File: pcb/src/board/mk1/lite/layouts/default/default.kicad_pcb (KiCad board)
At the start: 2 copper layers, 21 parts

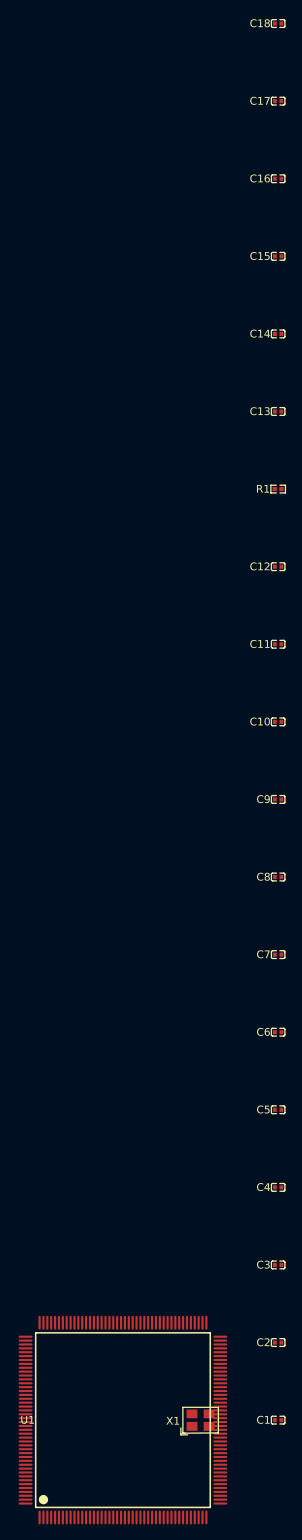
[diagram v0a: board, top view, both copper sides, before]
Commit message: pcb: add decoupling capacitors to STM32F429
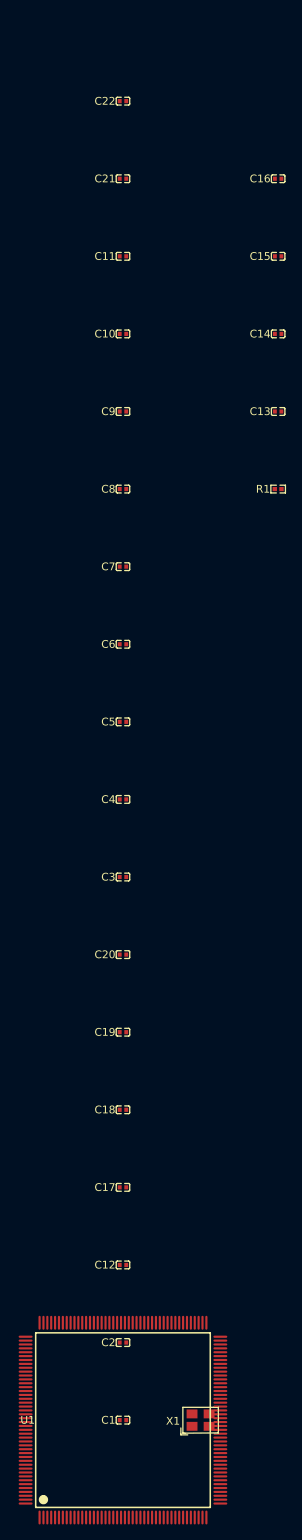
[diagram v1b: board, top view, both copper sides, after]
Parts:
- added C19: 100nF ±10%, Samsung_Electro_Mechanics_CL05B104KO5NNNC:C0402, F.Cu at (0.00, -50.0)
- added C20: 100nF ±10%, Samsung_Electro_Mechanics_CL05B104KO5NNNC:C0402, F.Cu at (0.00, -60.0)
- added C21: 1µF ±10%, Samsung_Electro_Mechanics_CL05A105KA5NQNC:C0402, F.Cu at (0.00, -160.0)
- added C22: 10nF ±10%, Samsung_Electro_Mechanics_CL05B103KB5NNNC:C0402, F.Cu at (0.00, -170.0)
- C1: value 100nF ±10% -> 4.7µF ±20%; footprint Samsung_Electro_Mechanics_CL05B104KO5NNNC:C0402 -> Samsung_Electro_Mechanics_CL05A475MP5NRNC:C0402
- C17: value 1µF ±10% -> 100nF ±10%; footprint Samsung_Electro_Mechanics_CL05A105KA5NQNC:C0402 -> Samsung_Electro_Mechanics_CL05B104KO5NNNC:C0402
- moved C17 141.4 mm to (0.00, -30.0)
- moved C18 141.4 mm to (0.00, -40.0)
- moved C12 92.2 mm to (0.00, -20.0)
- moved C10 53.9 mm to (0.00, -140.0)
- moved C11 53.9 mm to (0.00, -150.0)
- moved C3 53.9 mm to (0.00, -70.0)
- moved C4 53.9 mm to (0.00, -80.0)
- moved C5 53.9 mm to (0.00, -90.0)
- moved C6 53.9 mm to (0.00, -100.0)
- moved C7 53.9 mm to (0.00, -110.0)
- moved C8 53.9 mm to (0.00, -120.0)
- moved C9 53.9 mm to (0.00, -130.0)
- moved C1 20.0 mm to (0.00, 0.00)
- moved C2 20.0 mm to (0.00, -10.0)
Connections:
- C15 pad 1: vcap_caps[1]-power-hv -> vcap_caps[0]-power-hv
- U1 pad 125: 125 -> vcap_caps[1]-power-hv
- U1 pad 6: vbat-hv -> hv
- U1 pad 81: vcap_caps[1]-power-hv -> vcap_caps[0]-power-hv
